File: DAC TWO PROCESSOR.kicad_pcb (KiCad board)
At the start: 4 copper layers, 94 x 50.8 mm, 94 parts, among them J1 CONN_20, J2 CONN_10x2, J3 CONN_10, U1 ADP5070, U11 SM78L05, U12 SM79L05, U2 REG113-3.3, U4 ADP7118, U5 AT25160B, U6 ADP7182, U7 STM32F7xx

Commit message: EOD Push.
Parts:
- moved C15 83.9 mm to (142.2, 121.2)
- moved C4 76.7 mm to (142.2, 110.0)
- moved U2 73.6 mm to (142.2, 114.8), turned to 270 degrees
- moved C21 71.0 mm to (25.4, 134.1), turned to 270 degrees
- moved C29 68.9 mm to (27.2, 110.0), turned to 270 degrees
- moved C2 68.6 mm to (142.2, 112.5)
- moved R18 68.5 mm to (24.9, 110.7), turned to 180 degrees
- moved C24 67.8 mm to (20.6, 142.0), turned to 180 degrees
- moved C25 64.9 mm to (26.7, 151.4), turned to 90 degrees
- moved C13 64.9 mm to (142.2, 117.1)
- moved L1 60.9 mm to (79.5, 64.8), turned to 180 degrees
- moved R10 58.5 mm to (93.2, 63.0)
- moved C16 56.1 mm to (142.2, 118.6)
- moved C23 55.3 mm to (33.0, 151.4), turned to 90 degrees
- moved R17 52.7 mm to (24.9, 109.2)
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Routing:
- added copper zone on F.Cu, net 3.3V
- added copper zone on F.Cu, net DGND
- added copper zone on F.Cu, net Net-(C13-Pad1)
- added copper zone on F.Cu, net VCC

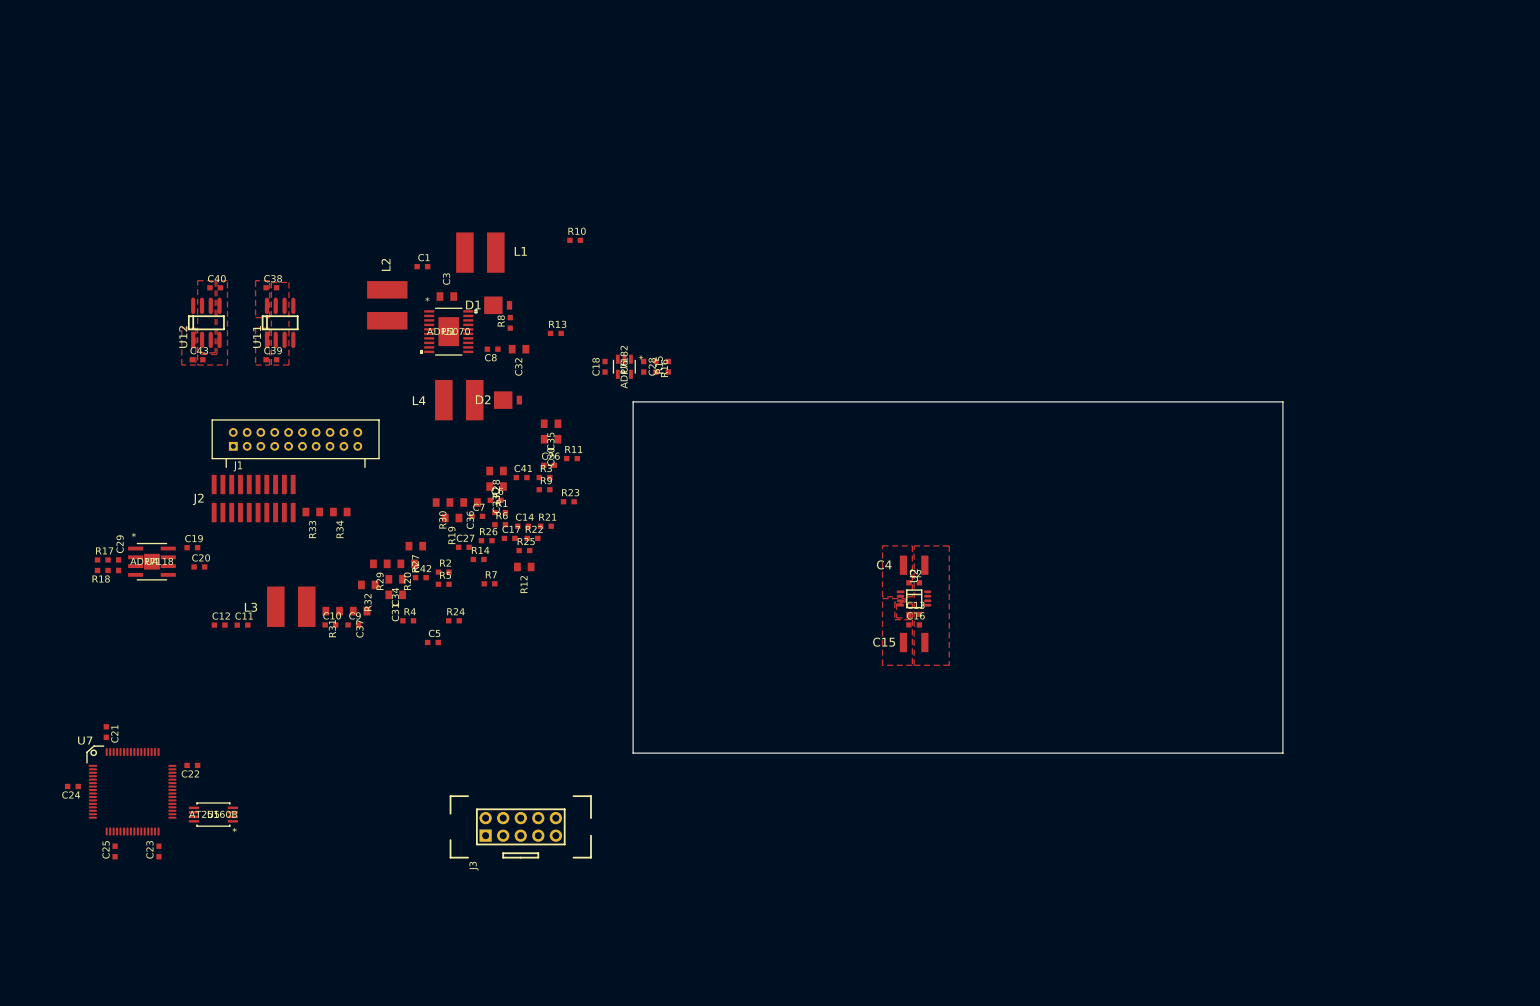
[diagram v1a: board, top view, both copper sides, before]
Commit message: Layed out some more power rails. Need to TRIPLE check the EPAD connections. Many are incorrectly pinned.
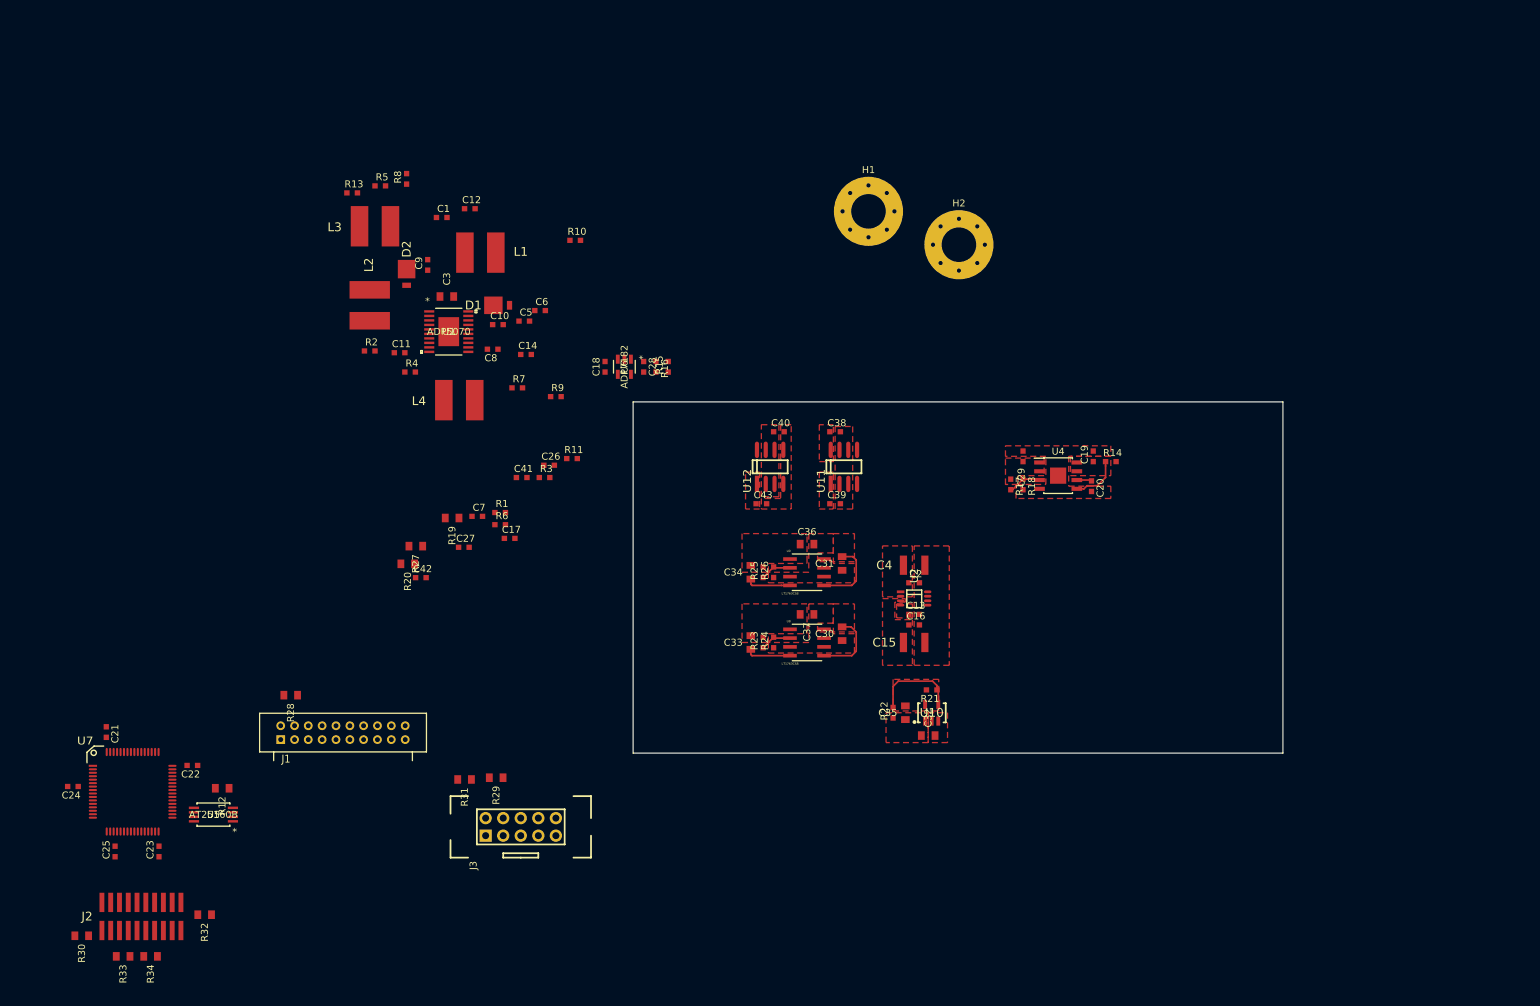
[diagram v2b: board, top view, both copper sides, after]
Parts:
- added H1: MountingHole_Pad, MountingHole:MountingHole_5mm_Pad_Via, F.Cu at (135.6, 58.8)
- added H2: MountingHole_Pad, MountingHole:MountingHole_5mm_Pad_Via, F.Cu at (148.7, 63.6)
- added U10: LT1964-SD, SciMod:SOT23-5, F.Cu at (144.8, 131.3)
- added U8: LT1763CS8, SciMod:SO-8_S, F.Cu at (126.7, 121.2)
- added U9: LT1763CS8, SciMod:SO-8_S, F.Cu at (126.7, 111.0)
- U4: footprint SciMod:ADP7118ARDZ -> Package_SO:SOIC-8-1EP_3.9x4.9mm_P1.27mm_EP2.35x2.35mm
- moved R18 133.7 mm to (158.0, 98.3), turned to 270 degrees
- moved R17 131.8 mm to (156.2, 98.3), turned to 270 degrees
- moved C29 131.8 mm to (158.0, 94.2), turned to 90 degrees
- moved U4 131.7 mm to (163.1, 97.0)
- moved C19 131.0 mm to (168.1, 94.2), turned to 90 degrees
- moved C20 129.6 mm to (167.9, 98.6), turned to 270 degrees
- moved R14 92.5 mm to (170.7, 95.0)
- moved U11 84.2 mm to (132.1, 95.8)
- moved C38 84.2 mm to (130.8, 90.7)
- moved C39 84.2 mm to (130.8, 101.1)
- moved C40 84.2 mm to (122.7, 90.7)
- moved C43 84.2 mm to (120.1, 101.1)
- moved U12 84.2 mm to (121.4, 95.8)
- moved R30 81.6 mm to (21.8, 163.6)
- moved C32 81.4 mm to (144.3, 134.6), turned to 180 degrees
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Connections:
- C33 pad 2: (no net) -> Net-(C33-Pad2)
- C34 pad 2: (no net) -> Net-(C34-Pad2)
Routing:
- net /VOUT1: track 0.00 -> 20.2 mm
- net Net-(R21-Pad1): track 0.00 -> 12.8 mm
- net Net-(C19-Pad1): track 0.00 -> 7.13 mm
- net Net-(C33-Pad2): track 0.00 -> 6.48 mm
- net Net-(C34-Pad2): track 0.00 -> 6.48 mm
- net Net-(R17-Pad2): track 0.00 -> 4.84 mm
- net Net-(R25-Pad1): track 0.00 -> 4.57 mm
- net Net-(R23-Pad1): track 0.00 -> 4.57 mm
- net Net-(C20-Pad1): track 0.00 -> 2.18 mm
- added copper zone on F.Cu, net +2.5V
- added copper zone on F.Cu, net +8V
- added copper zone on F.Cu, net -3V
- added copper zone on F.Cu, net /VOUT1
- added copper zone on F.Cu, net /VOUT2
- added copper zone on F.Cu, net AVDD
- added copper zone on F.Cu, net Net-(C19-Pad1)

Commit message: Moving components around that were changed due to annotation errors.
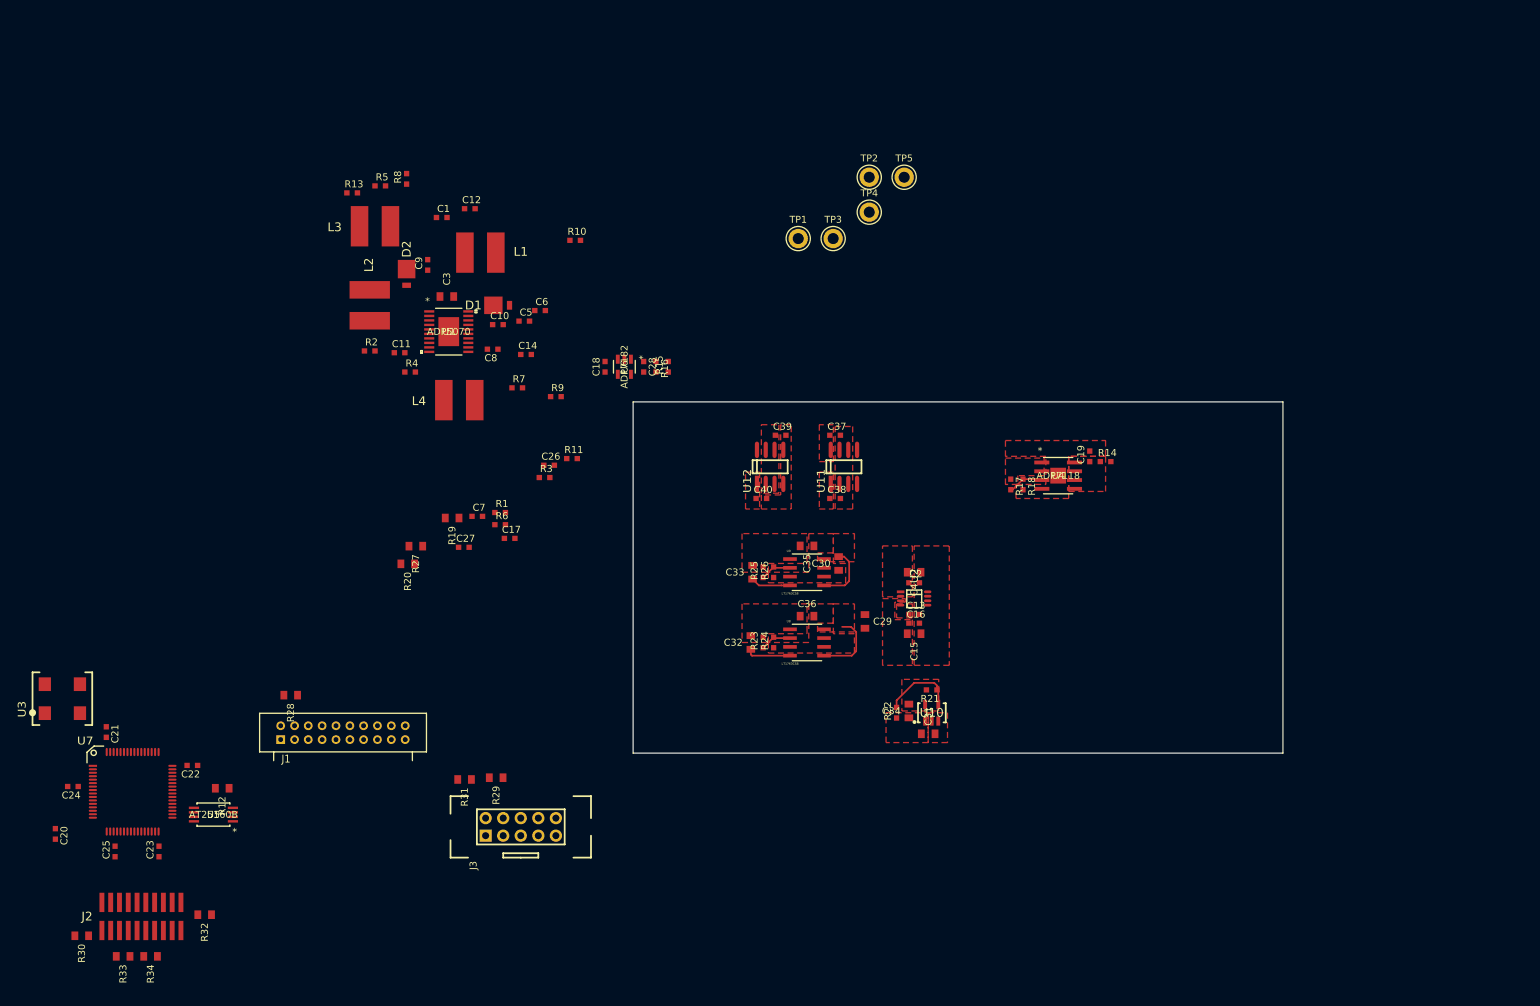
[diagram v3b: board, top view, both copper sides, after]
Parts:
- removed C41, C42: .1uF, SciMod:EIA0603
- removed C43: .33uF, SciMod:EIA0603
- removed H1, H2: MountingHole_Pad, MountingHole:MountingHole_5mm_Pad_Via
- added TP1: VOUT2, TestPoint:TestPoint_Keystone_5010-5014_Multipurpose, F.Cu at (125.5, 62.7)
- added TP2: VOUT1, TestPoint:TestPoint_Keystone_5010-5014_Multipurpose, F.Cu at (135.7, 53.9)
- added TP3: +2.5V, TestPoint:TestPoint_Keystone_5010-5014_Multipurpose, F.Cu at (130.5, 62.7)
- added TP4: +8V, TestPoint:TestPoint_Keystone_5010-5014_Multipurpose, F.Cu at (135.7, 58.9)
- added TP5: -3V, TestPoint:TestPoint_Keystone_5010-5014_Multipurpose, F.Cu at (140.8, 53.9)
- added U3: XX MHz, SciMod:CB3, F.Cu at (19.1, 129.3)
- C15, C4: footprint SciMod:EIA1210 -> SciMod:EIA0805
- C25: value .01uF -> 4.7uF
- C26: value 4.7uF -> .1uF
- C27: value .1uF -> 2.2uF
- C29: value 2.2uF -> 1uF; footprint SciMod:EIA0603 -> SciMod:EIA0805
- C32: value 1uF -> .01uF
- C34: value .01uF -> 10uF
- C37: value 10uF -> .33uF; footprint SciMod:EIA0805 -> SciMod:EIA0603
- U4: footprint Package_SO:SOIC-8-1EP_3.9x4.9mm_P1.27mm_EP2.35x2.35mm -> SciMod:ADP7118ARDZ
- moved C20 158.1 mm to (18.0, 148.8)
- moved C29 33.1 mm to (135.1, 118.1)
- moved C34 30.4 mm to (141.5, 131.1)
- moved C32 29.0 mm to (118.6, 121.2), turned to 270 degrees
- moved C35 28.0 mm to (126.7, 107.2), turned to 0 degrees
- moved C31 27.6 mm to (144.3, 134.4), turned to 180 degrees
- moved C37 26.2 mm to (130.8, 91.2)
- moved C39 12.7 mm to (122.9, 91.2)
- moved C36 10.4 mm to (126.7, 117.3)
- moved C30 10.2 mm to (131.3, 109.7)
- moved C33 10.2 mm to (118.9, 111.0)
- moved C40 9.98 mm to (120.1, 100.3)
- moved C38 9.65 mm to (130.8, 100.3)
- moved C15 1.27 mm to (142.2, 119.9)
- moved C4 1.02 mm to (142.2, 111.0)
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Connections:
- C20 pad 1: Net-(C20-Pad1) -> DGND
- C20 pad 2: AGND -> 3.3V
- C23 pad 1: DGND -> /EXT_NRST
- C23 pad 2: 3.3V -> DGND
- C24 pad 1: /EXT_NRST -> DGND
- C24 pad 2: DGND -> 3.3V
- C25 pad 1: DGND -> Net-(C25-Pad1)
- C25 pad 2: 3.3V -> DGND
- C26 pad 1: Net-(C26-Pad1) -> 3.3V
- C27 pad 1: 3.3V -> AVSS
- C27 pad 2: DGND -> AGND
- C28 pad 1: AVSS -> AVDD
- C29 pad 1: AVDD -> /VOUT1
- C31 pad 1: /VOUT1 -> /VOUT2
- C32 pad 1: /VOUT2 -> +2.5V
- C32 pad 2: AGND -> Net-(C32-Pad2)
- C33 pad 1: +2.5V -> +8V
- C34 pad 1: +8V -> -3V
- C34 pad 2: Net-(C34-Pad2) -> AGND
- C35 pad 1: -3V -> +8V
- C36 pad 1: +8V -> +2.5V
- C37 pad 1: +2.5V -> +12V
- C38 pad 1: +12V -> +5V
- C39 pad 1: +5V -> -12V
- C40 pad 1: -12V -> -5V
- U4 pad 6: Net-(C20-Pad1) -> (no net)
- U7 pad 30: Net-(C26-Pad1) -> Net-(C25-Pad1)
- U7 pad 5: (no net) -> Net-(U3-Pad3)
- U8 pad 4: Net-(C33-Pad2) -> Net-(C32-Pad2)
- U9 pad 4: Net-(C34-Pad2) -> Net-(C33-Pad2)
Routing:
- net Net-(C19-Pad1): track 7.13 -> 0.00 mm
- net Net-(C32-Pad2): track 0.00 -> 6.48 mm
- net Net-(C34-Pad2): track 6.48 -> 0.00 mm
- net /VOUT1: track 20.2 -> 18.1 mm
- net Net-(C20-Pad1): track 2.18 -> 0.00 mm
- net Net-(R21-Pad1): track 12.8 -> 10.9 mm
- net Net-(C33-Pad2): track 6.48 -> 5.79 mm

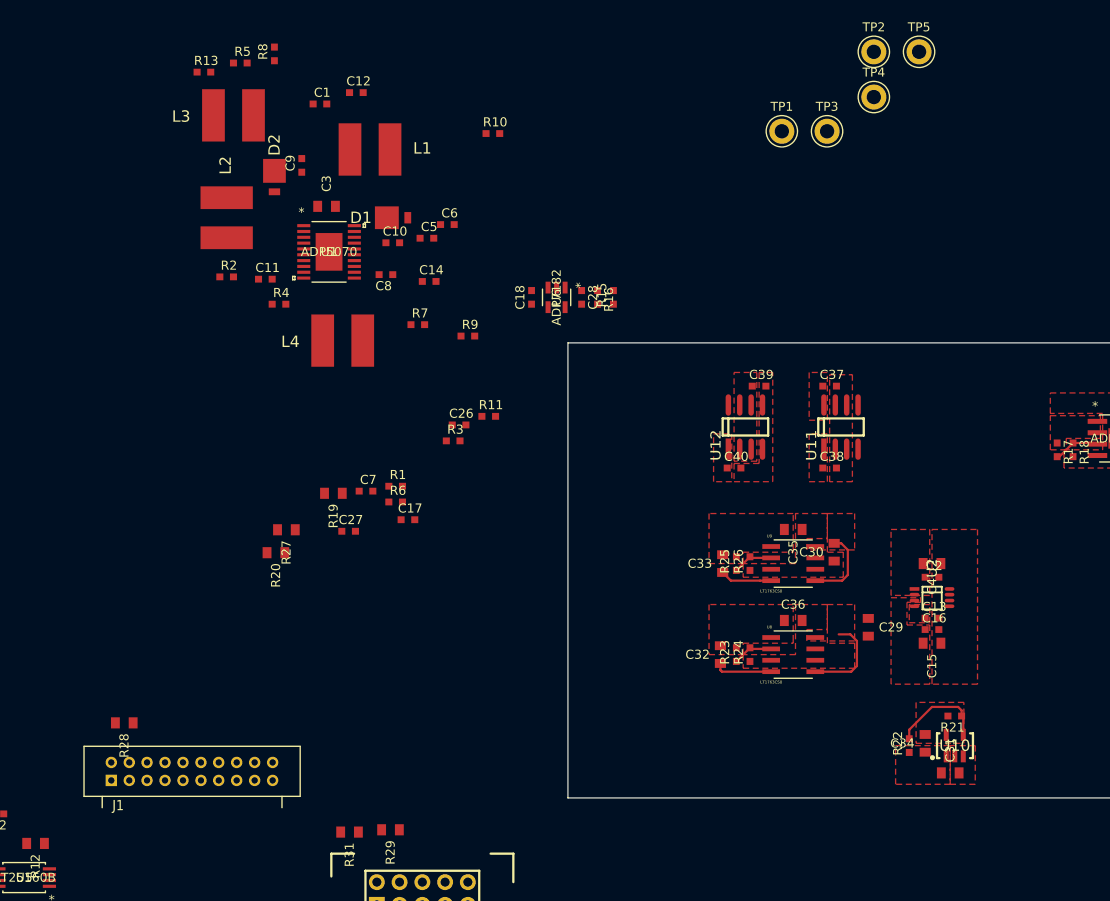
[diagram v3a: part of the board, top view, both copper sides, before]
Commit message: Good break point. Nearly finished ADP5070 layout. Just need uC layout and system positioning.
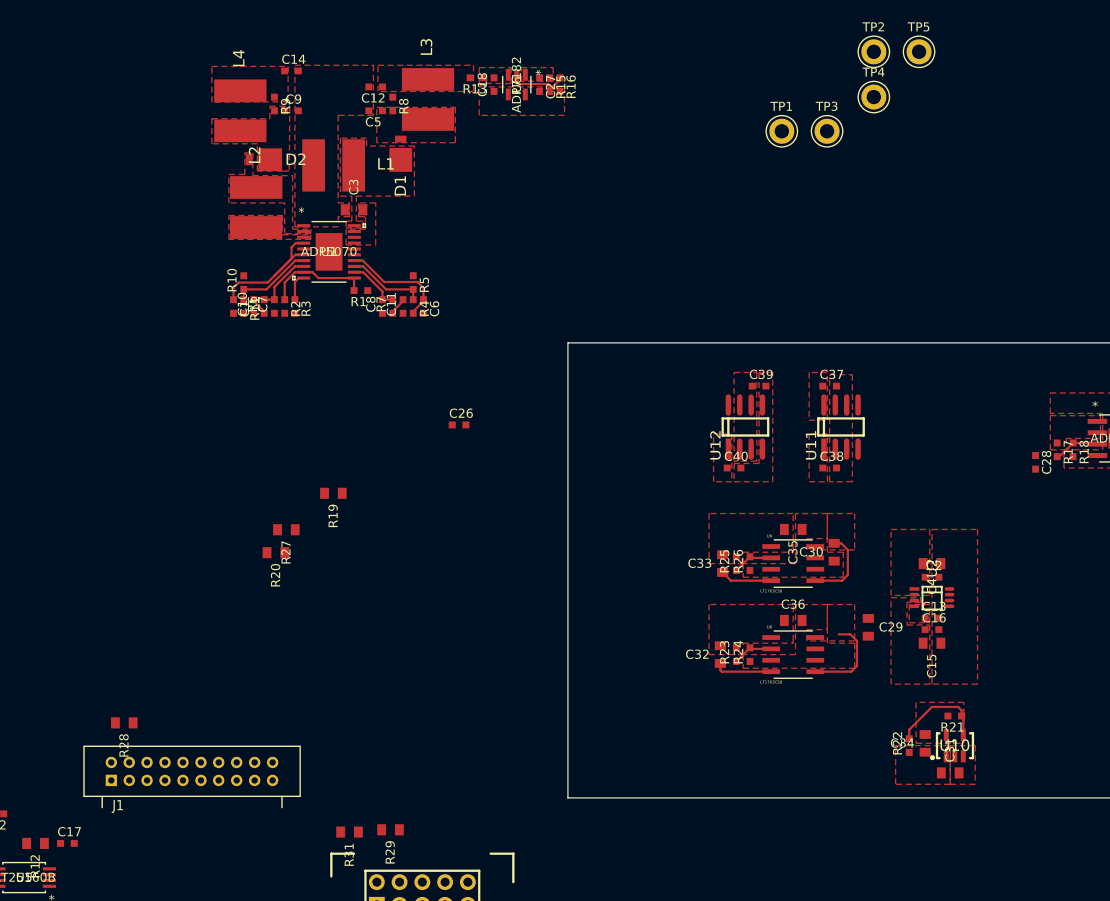
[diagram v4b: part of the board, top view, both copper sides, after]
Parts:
- moved C27 54.2 mm to (98.4, 57.5), turned to 270 degrees
- moved C28 53.9 mm to (153.8, 99.7)
- moved C17 52.5 mm to (45.7, 142.2)
- moved R9 33.7 mm to (68.8, 59.7), turned to 270 degrees
- moved R10 32.4 mm to (65.4, 79.6), turned to 90 degrees
- moved R5 31.2 mm to (84.3, 79.6), turned to 270 degrees
- moved R13 30.5 mm to (91.4, 56.8), turned to 180 degrees
- moved R11 30.0 mm to (65.4, 82.3), turned to 270 degrees
- moved L4 28.1 mm to (65.0, 60.5), turned to 270 degrees
- moved C14 28.1 mm to (70.7, 56.0)
- moved R6 26.3 mm to (67.7, 82.3), turned to 90 degrees
- moved R15 24.8 mm to (99.6, 57.5), turned to 270 degrees
- moved C1 24.6 mm to (64.3, 82.3), turned to 270 degrees
- moved U6 24.2 mm to (95.9, 57.5)
- moved C18 24.1 mm to (93.3, 57.5)
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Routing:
- net Net-(C1-Pad1): track 0.00 -> 16.2 mm
- net Net-(C6-Pad1): track 0.00 -> 12.3 mm
- net Net-(R1-Pad2): track 0.00 -> 11.8 mm
- net Net-(R10-Pad1): track 0.00 -> 9.18 mm
- net Net-(R4-Pad1): track 0.00 -> 8.78 mm
- net Net-(R15-Pad2): track 0.00 -> 7.36 mm
- net Net-(C7-Pad2): track 0.00 -> 6.82 mm
- net Net-(C8-Pad2): track 0.00 -> 6.08 mm
- net Net-(R3-Pad1): track 0.00 -> 3.14 mm
- net Net-(C11-Pad2): track 0.00 -> 2.00 mm
- net Net-(C10-Pad2): track 0.00 -> 2.00 mm
- added copper zone on F.Cu, net AVSS
- added copper zone on F.Cu, net CM_GND
- added copper zone on F.Cu, net Net-(C18-Pad1)
- added copper zone on F.Cu, net Net-(C5-Pad1)
- added copper zone on F.Cu, net Net-(C9-Pad1)
- added copper zone on F.Cu, net Net-(D1-Pad1)
- added copper zone on F.Cu, net Net-(D2-Pad2)
- added copper zone on F.Cu, net Net-(L2-Pad2)
